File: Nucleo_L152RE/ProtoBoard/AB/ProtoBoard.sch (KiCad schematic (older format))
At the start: 116 parts, among them CON1 USB-MICRO-B, J1 EXT1, J2 EXT2, J3 EXTPower, P1 Power, P10 OW2_A, P11 GND1, P12 I2C1_B, P13 I2C2_B, P14 SW_1_6, P15 WS1, P16 WS2, P17 MS2, P18 WS3, P19 WS4, P2 VinPower, P20 GND2, P21 Hole, P22 MS3, P23 OW3_A, P24 OW4_A, P25 MS4, P26 Hole, P27 Hole, P28 RGB1, P29 Ant, P3 USART2, P30 Hole, P4 SWD Header, P5 USART1, P6 MS1, P7 I2C1_A, P8 I2C2_A, P9 OW1_A, Q1 SI2323DS, SW1 MomentarySwitch, U2 Nucleo-L152RE-CN7, U3 Nucleo-L152RE-CN10, U5 MT3329_GPS, U6 S25FL127S, U7 RFM69HW

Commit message: Making more changes on Rev AB. Found that the voltage measurement circuit didn't work as expected, so it has been replaced with a voltage divider.  Removing second Ethernet port since they take up a lot of space and the utilization of it would probably be pretty low.  Corrected many errors from Rev AA.
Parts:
- removed C12: 0.1u, Capacitors_SMD:C_0603, symbol C
- removed J2: EXT2, nucleo:RJ45_SMD, symbol RJ45
- removed JP16, JP18, JP20, JP21, JP22, JP23, JP30, JP31, JP59: Jumper_NC_Small, nucleo:SB_NC, symbol Jumper_NC_Small
- removed JP17, JP19: Jumper_NO_Small, nucleo:SB_NO, symbol Jumper_NO_Small
- removed P19: WS4, Pin_Headers:Pin_Header_Straight_1x02, symbol CONN_01X02
- removed P24: OW4_A, Pin_Headers:Pin_Header_Straight_1x03, symbol CONN_01X03
- removed P28: RGB1, Pin_Headers:Pin_Header_Straight_1x04, symbol CONN_01X04
- removed Q1: SI2323DS, nucleo:TO-236, symbol Q_PMOS_GSD
- removed R1: 10K, Resistors_SMD:R_0603_HandSoldering, symbol R_Small
- removed R13, R38: 0, Resistors_SMD:R_0603_HandSoldering, symbol R_Small
- removed R39: 10k, Resistors_SMD:R_0603_HandSoldering, symbol R_Small
- removed R41: 4.7k, Resistors_SMD:R_0603_HandSoldering, symbol R_Small
- added C? (x2): 0.1u, Capacitors_SMD:C_0603_HandSoldering, symbol C_Small
- added C?: 10n, Capacitors_SMD:C_0603_HandSoldering, symbol C_Small
- added C? (x2): 1u, Capacitors_SMD:C_0603_HandSoldering, symbol C_Small
- added JP? (x2): Jumper_NC_Small, nucleo:SB_NC, symbol Jumper_NC_Small
- added JP? (x2): Jumper_NO_Small, nucleo:SB_NO, symbol Jumper_NO_Small
- added P?: Power3, Pin_Headers:Pin_Header_Straight_1x02, symbol CONN_01X02
- added P?: RGB1, symbol CONN_01X06
- added P?: Power1, Pin_Headers:Pin_Header_Straight_1x04, symbol CONN_01X04
- added R? (x5): 0, Resistors_SMD:R_0603_HandSoldering, symbol R_Small
- added R? (x2): 2.20k 1%, Resistors_SMD:R_0603_HandSoldering, symbol R_Small
- added R? (x2): 8.66k 1%, Resistors_SMD:R_0603_HandSoldering, symbol R_Small
- added U?: LDS3985, symbol LDS3985
- P1: value Power -> Power2
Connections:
- net labels added: 3.3ctl, 5V, RGB_CS, SensorVEnable, VIN_Meas1, VIN_Meas2
- net labels removed: EXT2_ADC, EXT2_GPIO, EXT2_SPI_CS, GPS_RX, GPS_TX, OneWireBus4, VIN_Meas, VIN_Trig, WS4
- no-connect marks 20 -> 24
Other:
- note added: "5V 3.5V to 5.5V\n Leaves Programmer Unpowered\n provided that JP5 is removed"
- note added: "Add 3.3V regulator for controlling\ni2c, motion sense, RGB spi, onewirebus, ext1"
- note added: "Can be used on Nucleo-L053R8 if\n X3 is an issue on 152re"
- note added: "Can choose between measuring 15V and 5V\n"
- note added: "Cell Voltage\n4.5V Max"
- note added: "E5V 3.5V to 5.5V\nAlso Powers ST-Link"
- note added: "I2C2 has a TX/RX pair that can be used for GPS"
- note added: "Make it so plugging in EXT1 into this one works"
- note added: "Max 130mA"
- note added: "Max 50mA"
- note added: "Modify sensor to output analog voltage if desired"
- note added: "Note: ADC also can do DAC"
- note added: "Pack Voltage\n4.5V Max"
- note added: "RGB LED, Spare SPI\n"
- note added: "SB62 and SB63 needed to be bridged\nfor USART2 to work."
- note added: "Switches, single ADC pin"
- note added: "Voltage Measurements\n"
- note removed: "Chip has the wrong pinout!\nNumbering Should have \nbeen correct (9 across from 8)"
- note removed: "E5V 3.5V to 5.5V"
- note removed: "Modify to read ADC voltage"
- note removed: "Note: GPIO also can do ADC, DAC"
- note removed: "RGB LED"
- note removed: "Switches, Digital Pin or ADC pin"
- note removed: "Voltage Measurement\nCan trigger and read within 1ms\nSee Jeelabs.org for details"
- moved on the sheet: C1, J1, J3, L3, L4, P1, P11, P15, P16, P18, P2, P20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

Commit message: Split schematic into multiple pages.  Added servo power input and calculated voltage dividers for ADC measurements with capacitors so that the measurements can be read by the ADC.
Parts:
- removed C1, C? (x2): 0.1u, Capacitors_SMD:C_0603_HandSoldering, symbol C_Small
- removed C10, C11, C8, C9: 0.1u, Capacitors_SMD:C_0603, symbol C
- removed C?: 10n, Capacitors_SMD:C_0603_HandSoldering, symbol C_Small
- removed C? (x2): 1u, Capacitors_SMD:C_0603_HandSoldering, symbol C_Small
- removed CON1: USB-MICRO-B, nucleo:USB_micro_AB, symbol USB-MICRO-B
- removed D1: Red, nucleo:LED_0603, symbol Led_Small
- removed D2: Yellow, nucleo:LED_0603, symbol Led_Small
- removed D3: Green, nucleo:LED_0603, symbol Led_Small
- removed D4: Blue, nucleo:LED_0603, symbol Led_Small
- removed J1: EXT1, nucleo:RJ45_SMD, symbol RJ45
- removed J3: EXTPower, nucleo:RJ45_SMD, symbol RJ45
- removed JP32, JP34, JP41, JP43, JP53, JP54, JP55, JP56, JP57, JP7, JP8, JP? (x2): Jumper_NC_Small, nucleo:SB_NC, symbol Jumper_NC_Small
- removed JP6, JP9, JP? (x2): Jumper_NO_Small, nucleo:SB_NO, symbol Jumper_NO_Small
- removed L3, L4: 600 Ohm, Resistors_SMD:R_0603_HandSoldering, symbol L_Small
- removed P1: Power2, Pin_Headers:Pin_Header_Straight_1x02, symbol CONN_01X02
- removed P10: OW2_A, Pin_Headers:Pin_Header_Straight_1x03, symbol CONN_01X03
- removed P11: GND1, Pin_Headers:Pin_Header_Straight_1x02, symbol CONN_01X02
- removed P12: I2C1_B, Pin_Headers:Pin_Header_Straight_1x04, symbol CONN_01X04
- removed P13: I2C2_B, Pin_Headers:Pin_Header_Straight_1x04, symbol CONN_01X04
- removed P14: SW_1_6, Pin_Headers:Pin_Header_Straight_2x06, symbol CONN_02X06
- removed P15: WS1, Pin_Headers:Pin_Header_Straight_1x02, symbol CONN_01X02
- removed P16: WS2, Pin_Headers:Pin_Header_Straight_1x02, symbol CONN_01X02
- removed P17: MS2, Pin_Headers:Pin_Header_Straight_1x03, symbol CONN_01X03
- removed P18: WS3, Pin_Headers:Pin_Header_Straight_1x02, symbol CONN_01X02
- removed P2: VinPower, Pin_Headers:Pin_Header_Straight_1x02, symbol CONN_01X02
- removed P20: GND2, Pin_Headers:Pin_Header_Straight_1x02, symbol CONN_01X02
- removed P22: MS3, Pin_Headers:Pin_Header_Straight_1x03, symbol CONN_01X03
- removed P23: OW3_A, Pin_Headers:Pin_Header_Straight_1x03, symbol CONN_01X03
- removed P25: MS4, Pin_Headers:Pin_Header_Straight_1x03, symbol CONN_01X03
- removed P29: Ant, Pin_Headers:Pin_Header_Straight_1x01, symbol CONN_01X01
- removed P3: USART2, Pin_Headers:Pin_Header_Straight_1x04, symbol CONN_01X04
- removed P4: SWD Header, Pin_Headers:Pin_Header_Straight_1x06, symbol CONN_01X06
- removed P5: USART1, Pin_Headers:Pin_Header_Straight_1x04, symbol CONN_01X04
- removed P6: MS1, Pin_Headers:Pin_Header_Straight_1x03, symbol CONN_01X03
- removed P7: I2C1_A, Pin_Headers:Pin_Header_Straight_1x04, symbol CONN_01X04
- removed P8: I2C2_A, Pin_Headers:Pin_Header_Straight_1x04, symbol CONN_01X04
- removed P9: OW1_A, Pin_Headers:Pin_Header_Straight_1x03, symbol CONN_01X03
- removed P?: Power3, Pin_Headers:Pin_Header_Straight_1x02, symbol CONN_01X02
- removed P?: RGB1, symbol CONN_01X06
- removed P?: Power1, Pin_Headers:Pin_Header_Straight_1x04, symbol CONN_01X04
- removed R10, R8, R9: 1k, Resistors_SMD:R_0603_HandSoldering, symbol R_Small
- removed R11, R35, R36, R37, R4, R6, R? (x5): 0, Resistors_SMD:R_0603_HandSoldering, symbol R_Small
- removed R12, R5: 33, Resistors_SMD:R_0603_HandSoldering, symbol R_Small
- removed R14, R16: 100k, Resistors_SMD:R_0603_HandSoldering, symbol R_Small
- removed R15, R21: 10k, Resistors_SMD:R_0603_HandSoldering, symbol R_Small
- removed R17, R18, R19, R20: 2.2k, Resistors_SMD:R_0603_HandSoldering, symbol R_Small
- removed R2, R? (x2): 2.20k 1%, Resistors_SMD:R_0603_HandSoldering, symbol R_Small
- removed R22: 4.7K, Resistors_SMD:R_0603_HandSoldering, symbol R_Small
- removed R23: 2.2K, Resistors_SMD:R_0603_HandSoldering, symbol R_Small
- removed R24: 680, Resistors_SMD:R_0603_HandSoldering, symbol R_Small
- removed R25: 390, Resistors_SMD:R_0603_HandSoldering, symbol R_Small
- removed R26, R27, R40: 4.7k, Resistors_SMD:R_0603_HandSoldering, symbol R_Small
- removed R28, R42, R43, R44: 220, Resistors_SMD:R_0603_HandSoldering, symbol R_Small
- removed R3, R? (x2): 8.66k 1%, Resistors_SMD:R_0603_HandSoldering, symbol R_Small
- removed R7: 1K, Resistors_SMD:R_0603_HandSoldering, symbol R_Small
- removed SW1: MomentarySwitch, nucleo:Tact_switch, symbol MomentarySwitch
- removed U2: Nucleo-L152RE-CN7, Pin_Headers:Pin_Header_Straight_2x19, symbol Nucleo-L152RE-CN7
- removed U3: Nucleo-L152RE-CN10, Pin_Headers:Pin_Header_Straight_2x19, symbol Nucleo-L152RE-CN10
- removed U5: MT3329_GPS, nucleo:MT3329, symbol MT3329_GPS
- removed U6: S25FL127S, nucleo:SOIC-8-FLASH, symbol S25FL127S
- removed U7: RFM69HW, nucleo:RFM69HW, symbol RFM69HW
- removed U?: LDS3985, symbol LDS3985
- added P5: GND1, Pin_Headers:Pin_Header_Straight_1x02, symbol CONN_01X02
- added P6: GND2, Pin_Headers:Pin_Header_Straight_1x02, symbol CONN_01X02
- renumbered P21 to P1, P26 to P2, P27 to P3, P30 to P4
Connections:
- net GND: now also P5.1 (P1), P5.2 (P2), P6.1 (P1), P6.2 (P2)
- no-connect marks 24 -> 1
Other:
- note added: "Ground Connections"
- note added: "Lower Voltage, Lower Current, Upper Current:\n RFM69HW - 2.4V\n MT3329 - 3.2V (50mVpp ripple)\n S25FL127S - 2.7V\n\n"
- note added: "Rev AA Errata 4-26-2015:\n U2: Pin 9, 11 No Connection\n U3: Pin 10: No Connection\n Pin 36: No Connection\n Pin 38: No Connection"
- note removed: "3.3V Only"
- note removed: "3.3v en"
- note removed: "5V 3.5V to 5.5V\n Leaves Programmer Unpowered\n provided that JP5 is removed"
- note removed: "Add 3.3V regulator for controlling\ni2c, motion sense, RGB spi, onewirebus, ext1"
- note removed: "Can be powered from USB if\n U5V connected\nCan Provide power to USB if\n E5V connected"
- note removed: "Can be used on Nucleo-L053R8 if\n X3 is an issue on 152re"
- note removed: "Can choose between measuring 15V and 5V\n"
- note removed: "Cell Voltage\n4.5V Max"
- note removed: "Connect when ST-Link is disconnected"
- note removed: "Current Sensing Adapter"
- note removed: "DAC1"
- note removed: "DAC2"
- note removed: "Digital Temperature Sensor\n"
- note removed: "Divide down\n15 to 3.3v"
- note removed: "E5V 3.5V to 5.5V\nAlso Powers ST-Link"
- note removed: "Ensure GPIO or ADC chosen\ncan be source of interrupts"
- note removed: "Expansion port for Power"
- note removed: "Extra GPIO from wireless\nmodule is brought to header\n"
- note removed: "Flash Storage"
- note removed: "Future boards can be powered\nusing this pin"
- note removed: "GPS MT3339"
- note removed: "I2C Devices"
- note removed: "I2C2 has a TX/RX pair that can be used for GPS"
- note removed: "Idea seems simple, but implementation is complicated.\nBetter to make a stand alone system that can perform\nthe measurements and return them to us."
- note removed: "Ideally we could connect DPlus and DMinus\nTo a USB port"
- note removed: "If using E5V, won't be able to turn off i2c devices"
- note removed: "If we are using USB\nstatus 2 not as important."
- note removed: "KICAD won't find unconnected nets\n"
- note removed: "Make it so plugging in EXT1 into this one works"
- note removed: "Max 130mA"
- note removed: "Max 50mA"
- note removed: "Modify sensor to output analog voltage if desired"
- note removed: "Motion Sensor (modify Sensor to run at 3.3), output 1 or 0"
- note removed: "Not 5V Tolerant: PC3, PA3, PA4, PA5, PB0"
- note removed: "Note: ADC also can do DAC"
- note removed: "PWM"
- note removed: "Pack Voltage\n4.5V Max"
- note removed: "RGB LED, Spare SPI\n"
- note removed: "Rev AA Errata 4-26-2015:\nU2: Pin 9, 11 No Connection\nU3: Pin 10: No Connection\n Pin 36: No Connection\n Pin 38: No Connection"
- note removed: "SB62 and SB63 needed to be bridged\nfor USART2 to work."
- note removed: "SPI Bus"
- note removed: "STLINK - Open OCD Connection"
- note removed: "SWO"
- note removed: "Select PWM pins\nTweak Res"
- note removed: "Since GPS will only be populated on a few units\n Use those lines for Status indicators"
- note removed: "StatusLed2 Shares pin with \nUSB ID pin"
- note removed: "StatusLed3 Shares pin with \nGPS Enable"
- note removed: "StatusLed4 Shares pin with \nEXT 3.3V en"
- note removed: "Switches, single ADC pin"
- note removed: "TCK"
- note removed: "TMS"
- note removed: "Theory Behind this circuit\nis to be able to measure multiple\nbutton or switch presses on one\nADC pin"
- note removed: "U5V should be not connected \nwhen USB is plugged in"
- note removed: "Using a MAX4239 with a ADS1240"
- note removed: "Vin 6.5 to 15v"
- note removed: "Voltage Measurements\n"
- note removed: "Water Sensors, ADC Pins"
- note removed: "Wireless"
- moved on the sheet: P1, P2, P3, P4, S1

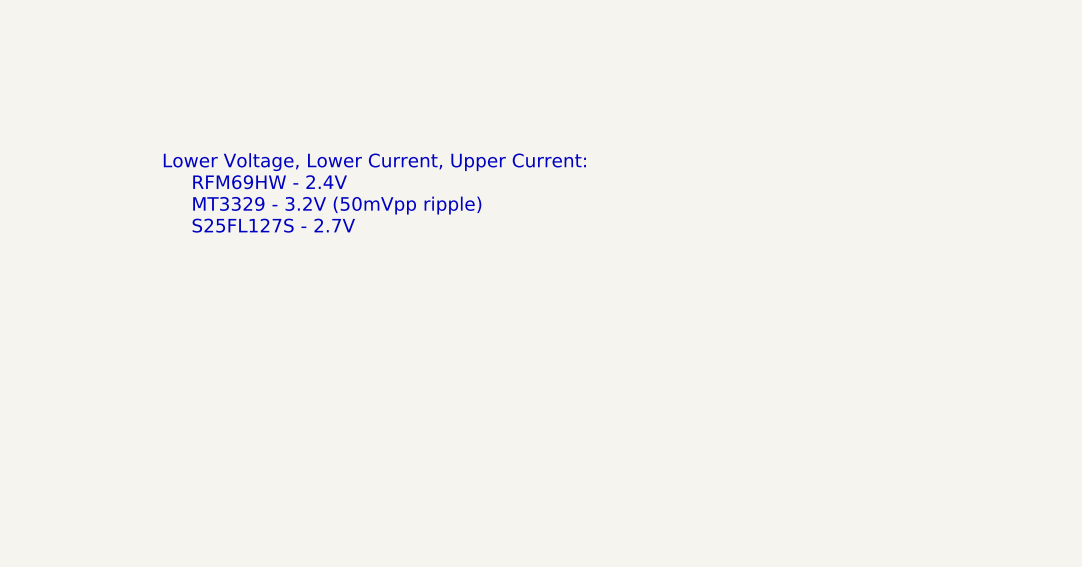
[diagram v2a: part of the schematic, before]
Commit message: Components mostly laid out into final resting positions with exception of plethora of single pin connections for easily connecting to GND, 3.3V, 5V, 3.3Vctl.
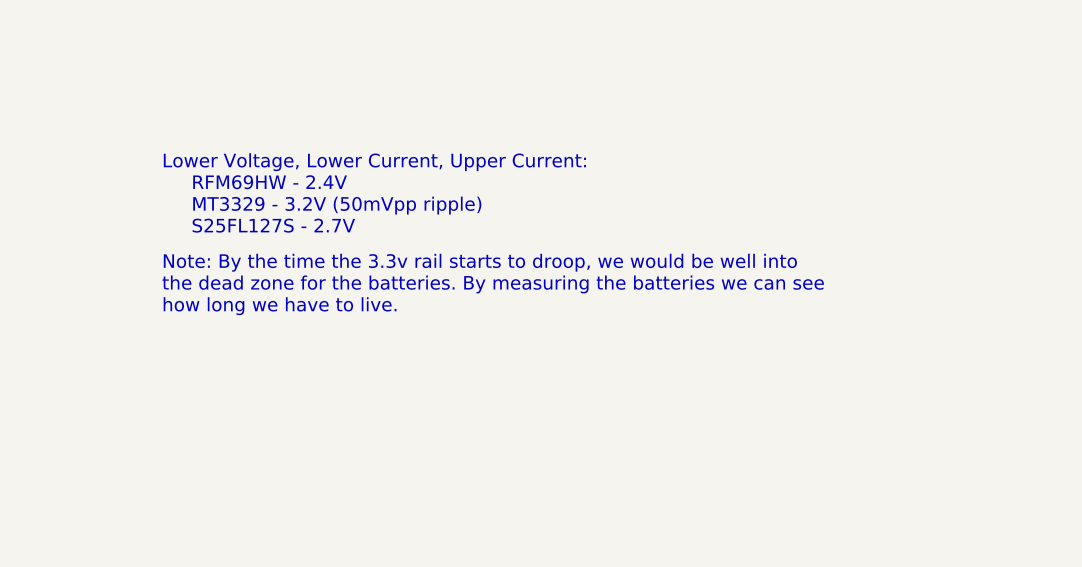
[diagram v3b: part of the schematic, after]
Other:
- note added: "Note: By the time the 3.3v rail starts to droop, we would be well into\nthe dead zone for the batteries. By measuring the batteries we can see\nhow long we have to live."
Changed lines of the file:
@@
 Sheet 1 5
 Title "Expansion Board For STM32 Nucleo-L152RE"
-Date "Sunday, May 24 , 2015"
-Rev "AB"
+Date "Saturday, May 23, 2015"
+Rev "AB - Draft"
 Comp "Open Source Hardware"
 Comment1 "MIT License"
@@
 Text Notes 6300 1700 0    59   ~ 0
 Lower Voltage, Lower Current, Upper Current:\n     RFM69HW - 2.4V\n     MT3329 - 3.2V (50mVpp ripple)\n     S25FL127S - 2.7V\n\n
+Text Notes 6300 1950 0    59   ~ 0
+Note: By the time the 3.3v rail starts to droop, we would be well into\nthe dead zone for the batteries. By measuring the batteries we can see\nhow long we have to live.
 $EndSCHEMATC

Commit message: Final draft with all traces and artwork in place.
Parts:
- removed P1, P2, P3: Hole, nucleo:plat_hole_4_20, symbol CONN_01X01
- removed P4: Hole, Mounting_Holes:MountingHole_3mm, symbol CONN_01X01
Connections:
- no-connect marks 1 -> 0
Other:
- note removed: "Rev AA Errata 4-26-2015:\n U2: Pin 9, 11 No Connection\n U3: Pin 10: No Connection\n Pin 36: No Connection\n Pin 38: No Connection"
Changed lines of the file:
@@
 Sheet 1 5
 Title "Expansion Board For STM32 Nucleo-L152RE"
-Date "Saturday, May 23, 2015"
-Rev "AB - Draft"
+Date "Sunday, May 31, 2015"
+Rev "AB - Final Draft"
 Comp "Open Source Hardware"
 Comment1 "MIT License"
@@
 Comment4 ""
 $EndDescr
-Text Notes 1800 1200 2    60   ~ 0
+Text Notes 1600 1650 2    60   ~ 0
 Potential Cases:\n    Hammond HM1071-ND
-$Comp
-L CONN_01X01 P1
-U 1 1 552D67CC
-P 1850 4150
-F 0 "P1" H 1850 4250 50  0000 C CNN
-F 1 "Hole" V 1950 4150 50  0000 C CNN
-F 2 "nucleo:plat_hole_4_20" H 1850 4150 60  0001 C CNN
-F 3 "" H 1850 4150 60  0000 C CNN
-	1    1850 4150
-	1    0    0    -1
-$EndComp
-$Comp
-L GND #PWR01
-U 1 1 552D72B3
-P 1650 4550
-F 0 "#PWR01" H 1650 4300 50  0001 C CNN
-F 1 "GND" H 1650 4400 50  0000 C CNN
-F 2 "" H 1650 4550 60  0000 C CNN
-F 3 "" H 1650 4550 60  0000 C CNN
-	1    1650 4550
-	1    0    0    -1
-$EndComp
-$Comp
-L CONN_01X01 P2
-U 1 1 552D814E
-P 1850 4350
-F 0 "P2" H 1850 4450 50  0000 C CNN
-F 1 "Hole" V 1950 4350 50  0000 C CNN
-F 2 "nucleo:plat_hole_4_20" H 1850 4350 60  0001 C CNN
-F 3 "" H 1850 4350 60  0000 C CNN
-	1    1850 4350
-	1    0    0    -1
-$EndComp
-$Comp
-L CONN_01X01 P3
-U 1 1 552D8244
-P 1850 4550
-F 0 "P3" H 1850 4650 50  0000 C CNN
-F 1 "Hole" V 1950 4550 50  0000 C CNN
-F 2 "nucleo:plat_hole_4_20" H 1850 4550 60  0001 C CNN
-F 3 "" H 1850 4550 60  0000 C CNN
-	1    1850 4550
-	1    0    0    -1
-$EndComp
-$Comp
-L CONN_01X01 P4
-U 1 1 552D833C
-P 2400 4150
-F 0 "P4" H 2400 4250 50  0000 C CNN
-F 1 "Hole" V 2500 4150 50  0000 C CNN
-F 2 "Mounting_Holes:MountingHole_3mm" H 2400 4150 60  0001 C CNN
-F 3 "" H 2400 4150 60  0000 C CNN
-	1    2400 4150
-	1    0    0    -1
-$EndComp
-NoConn ~ 2200 4150
 $Comp
 L Symbol S1
@@
 	1    0    0    -1
 $EndComp
-Text Notes 550  950  0    59   ~ 0
-Rev AA Errata 4-26-2015:\n  U2: Pin 9, 11 No Connection\n  U3: Pin 10: No Connection\n       Pin 36: No Connection\n       Pin 38: No Connection
-Connection ~ 1650 4350
-Wire Wire Line
-	1650 4150 1650 4550
 $Sheet
 S 1550 3050 1250 450
@@
 $EndComp
 $Comp
-L GND #PWR02
+L GND #PWR01
 U 1 1 555D860C
 P 2300 4900
-F 0 "#PWR02" H 2300 4650 50  0001 C CNN
+F 0 "#PWR01" H 2300 4650 50  0001 C CNN
 F 1 "GND" H 2300 4750 50  0000 C CNN
 F 2 "" H 2300 4900 60  0000 C CNN
@@
 $EndComp
 $Comp
-L GND #PWR03
+L GND #PWR02
 U 1 1 555D8612
 P 2800 4900
-F 0 "#PWR03" H 2800 4650 50  0001 C CNN
+F 0 "#PWR02" H 2800 4650 50  0001 C CNN
 F 1 "GND" H 2800 4750 50  0000 C CNN
 F 2 "" H 2800 4900 60  0000 C CNN
